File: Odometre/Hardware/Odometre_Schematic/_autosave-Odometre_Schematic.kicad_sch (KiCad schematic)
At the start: 9 parts, among them IC1 STM32C092FCP6, J1 Conn_01x04_Pin, J2 Conn_01x08_Pin, U1 MCP2562-E-SN, U2 LM1117DT-3.3

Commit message: autosave kicad
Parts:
- added C1, C2: 10µF, symbol Device:C_Small
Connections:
- net +3.3V: now also C2.1
- net GND: now also C1.2, C2.2
- net FDCAN1_RX: now reaches U1.1 (TXD)
- net FDCAN1_RX: now also IC1.15 (FDCAN1_RX)
- net FDCAN1_TX: now reaches U1.4 (RXD)
- net FDCAN1_TX: now also IC1.20 (FDCAN1_TX)
- net USART1_RX: now reaches IC1.1 (USART1_RX)
- net USART2_RX: now reaches IC1.10 (USART2_RX)
- net LED_MOTEUR: now reaches IC1.12 (GPIO_Output)
- net Green_LED: now reaches IC1.16 (GPIO_Output)
- net BOUTON: now reaches IC1.17 (GPIO_Input)
- net DEBUG_SWDIO: now reaches IC1.18 (DEBUG_SWDIO)
- net DEBUG_SWCLK: now reaches IC1.19 (DEBUG_SWCLK)
- net USART1_TX: now reaches IC1.2 (USART1_TX)
- net TIM2_CH1: now reaches IC1.7 (TIM2_CH1)
- net TIM2_CH2: now reaches IC1.8 (TIM2_CH2)
- net USART2_TX: now reaches IC1.9 (USART2_TX)
- net +12V renamed +5V
- net +5V: now also C1.1
- no-connect marks 0 -> 5

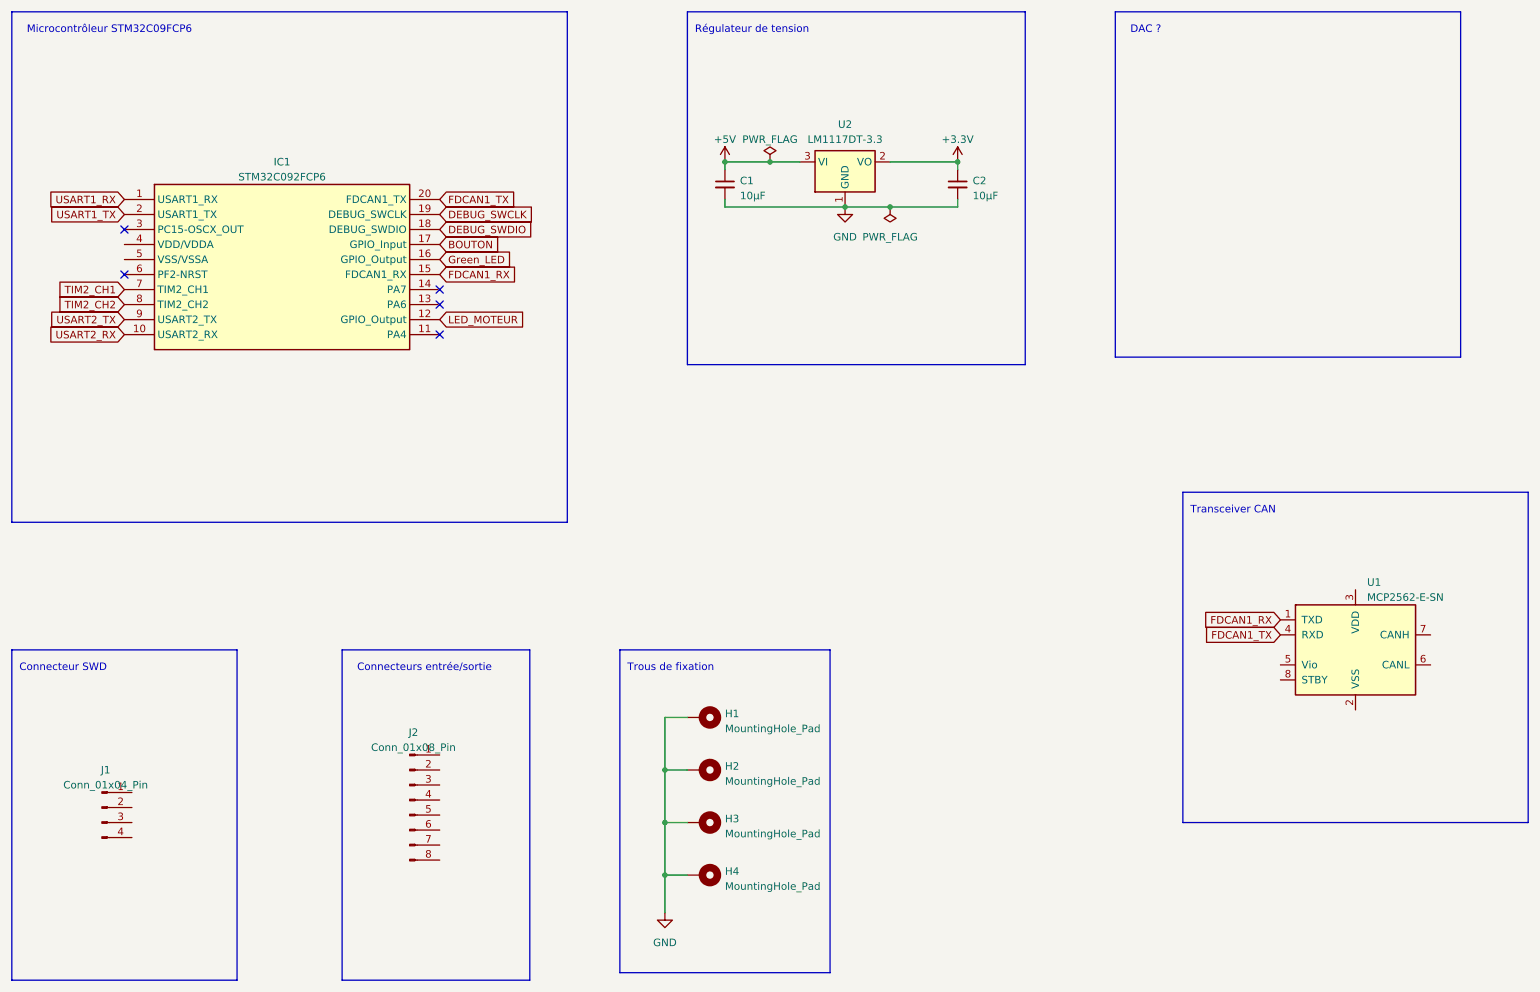
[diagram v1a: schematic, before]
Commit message: modification
suppression d'un pin gpio input
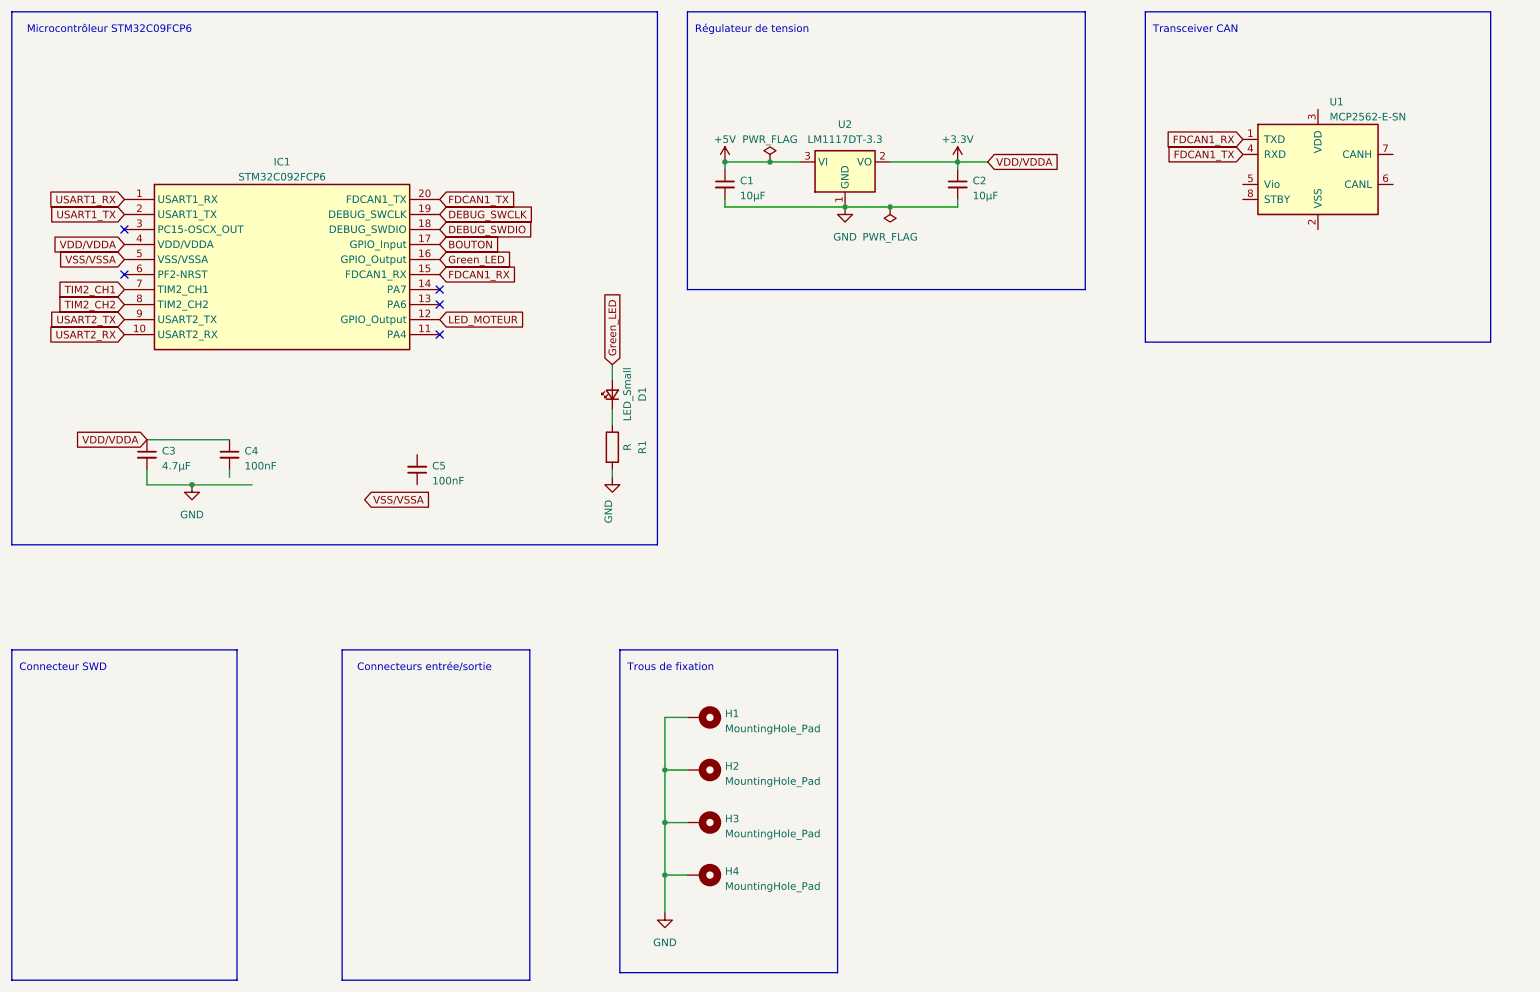
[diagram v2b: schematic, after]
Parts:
- removed J1: Conn_01x04_Pin, symbol Connector:Conn_01x04_Pin
- removed J2: Conn_01x08_Pin, symbol Connector:Conn_01x08_Pin
- added C3: 4.7µF, symbol Device:C_Small
- added C4, C5: 100nF, symbol Device:C_Small
- added D1: LED_Small, symbol Device:LED_Small
- added R1: R, symbol Device:R
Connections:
- net +3.3V: now also IC1.4 (VDD/VDDA), C3.1, C4.1
- net GND: now also C3.2, R1.2
- net Green_LED: now also D1.2 (A)
- net VSS/VSSA: now reaches IC1.5 (VSS/VSSA)
- new net: D1.1 (K), R1.1
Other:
- note removed: "DAC ?"
- moved on the sheet: U1
